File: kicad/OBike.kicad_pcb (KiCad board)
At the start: 2 copper layers, 60 x 60 mm, 59 parts, among them J1 Conn_01x04, J3 Conn_01x02, J4 Conn_01x03, J5 Conn_01x08, J7 Conn_01x04, J8 Micro_SD_Card_Det1, SW1 5_position_tactile, U1 DPS368XTSA1, U2 DS3231M, U3 MCP23017_SO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

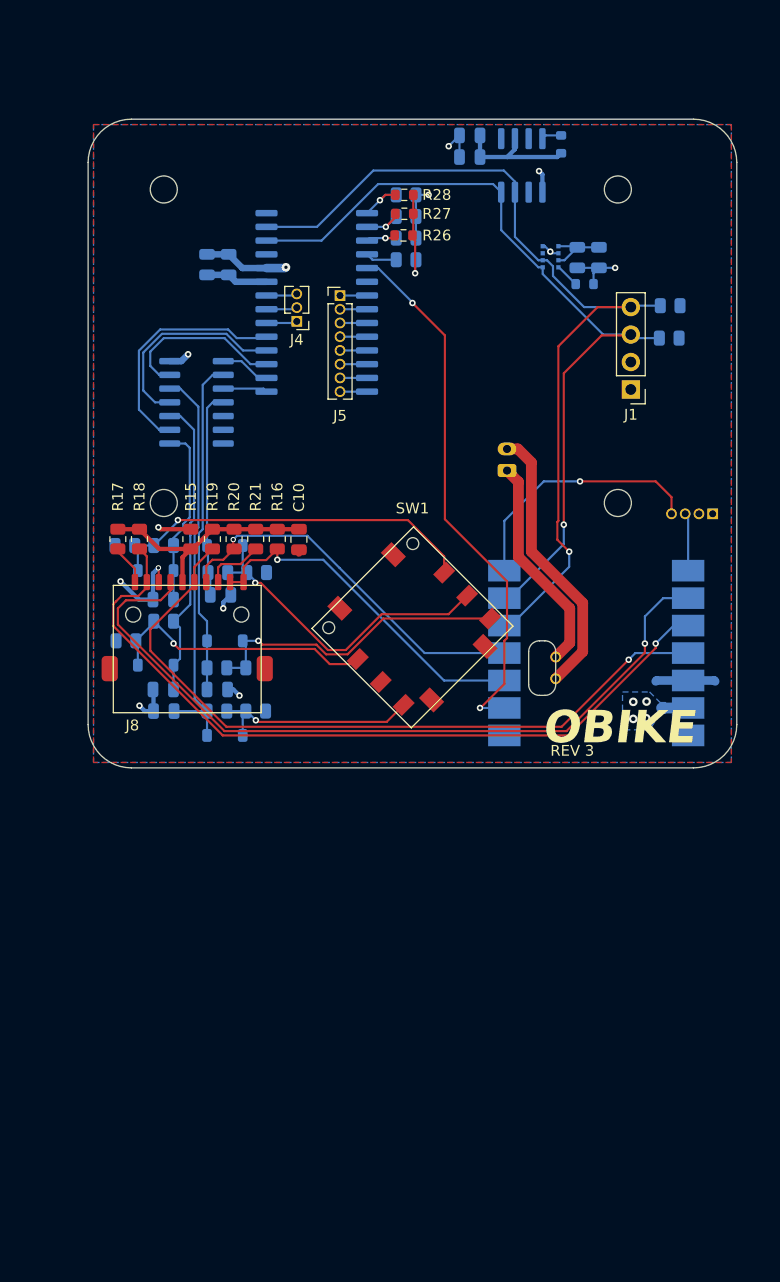
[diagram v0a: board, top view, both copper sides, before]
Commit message: 1.69" TFT
Changed screen connections to suit an SPI screen
Changed the arduino project to use the adafruit ST7789 library
Intended LCD is the wavshare 1.69" LCD
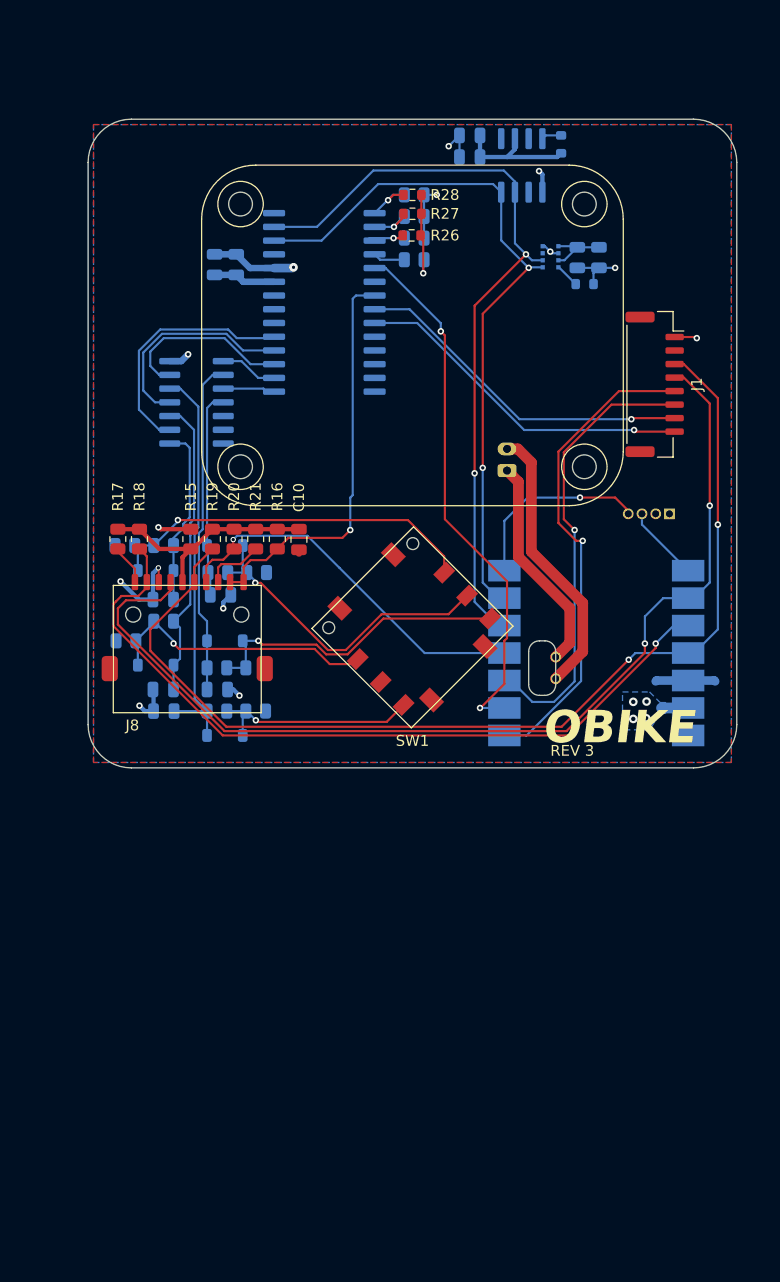
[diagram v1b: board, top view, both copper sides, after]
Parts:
- removed J4: Conn_01x03, Connector_PinHeader_1.27mm:PinHeader_1x03_P1.27mm_Vertical
- removed J5: Conn_01x08, Connector_PinHeader_1.27mm:PinHeader_1x08_P1.27mm_Vertical
- removed R11, R12: 10K, Resistor_SMD:R_0805_2012Metric
- J1: value Conn_01x04 -> Conn_01x08; footprint Connector_PinHeader_2.54mm:PinHeader_1x04_P2.54mm_Vertical -> Connector_JST:JST_GH_SM08B-GHS-TB_1x08-1MP_P1.25mm_Horizontal
- moved J7 4.00 mm to (176.3, 82.0)
- moved J1 2.25 mm to (174.9, 70.0), turned to -90 degrees
- moved R22 0.75 mm to (152.7, 58.5)
- moved R23 0.75 mm to (152.7, 52.5)
- moved R24 0.75 mm to (152.7, 54.5)
- moved R25 0.75 mm to (152.7, 56.5)
- moved R26 0.75 mm to (152.4, 56.2)
- moved R27 0.75 mm to (152.5, 54.2)
- moved R28 0.75 mm to (152.5, 52.5)
- moved C11 0.70 mm to (136.2, 59.0)
- moved C12 0.70 mm to (134.2, 59.0)
- moved U3 0.70 mm to (144.3, 62.4)
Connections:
- net CS renamed SD_CS
- J1 pad 3: SCL -> MOSI
- J1 pad 4: SDA -> SCK
- U3 pad 21: Net-(J5-Pin_1) -> DET
- U3 pad 22: Net-(J5-Pin_2) -> SCR_RST
- U3 pad 23: Net-(J5-Pin_3) -> SCR_BL
- U3 pad 24: Net-(J5-Pin_4) -> unconnected-(U3-GPA3-Pad24)
- U3 pad 25: Net-(J5-Pin_5) -> unconnected-(U3-GPA4-Pad25)
- U3 pad 26: Net-(J5-Pin_6) -> unconnected-(U3-GPA5-Pad26)
- U3 pad 27: Net-(J5-Pin_7) -> unconnected-(U3-GPA6-Pad27)
- U3 pad 28: Net-(J5-Pin_8) -> unconnected-(U3-GPA7-Pad28)
- U5 pad 1: unconnected-(U5-PA02_A0_D0-Pad1) -> SCR_CS
- U5 pad 3: DET -> SCR_DC
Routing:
- net SCR_CS: track 0.00 -> 44.8 mm, vias 0 -> 1
- net SCR_DC: track 0.00 -> 41.8 mm, vias 0 -> 1
- net SCR_RST: track 0.00 -> 32.7 mm, vias 0 -> 1
- net SCR_BL: track 0.00 -> 32.6 mm, vias 0 -> 1
- net MOSI: track 67.3 -> 97.6 mm, vias 1 -> 2
- net SCK: track 71.7 -> 95.1 mm, vias 1 -> 2
- net SDA: track 86.1 -> 72.3 mm, vias 1 -> 2
- net SCL: track 77.9 -> 67.0 mm, vias 1 -> 2
- net TX: track 23.7 -> 17.8 mm
- net DET: track 33.3 -> 37.0 mm
- net Net-(J4-Pin_3): track 2.86 -> 0.00 mm
- net Net-(J4-Pin_2): track 2.86 -> 0.00 mm
- net Net-(J4-Pin_1): track 2.86 -> 0.00 mm
- net Net-(J5-Pin_8): track 2.50 -> 0.00 mm
- net Net-(J5-Pin_7): track 2.50 -> 0.00 mm
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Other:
- outline, holes or cut-outs redrawn

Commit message: gps added
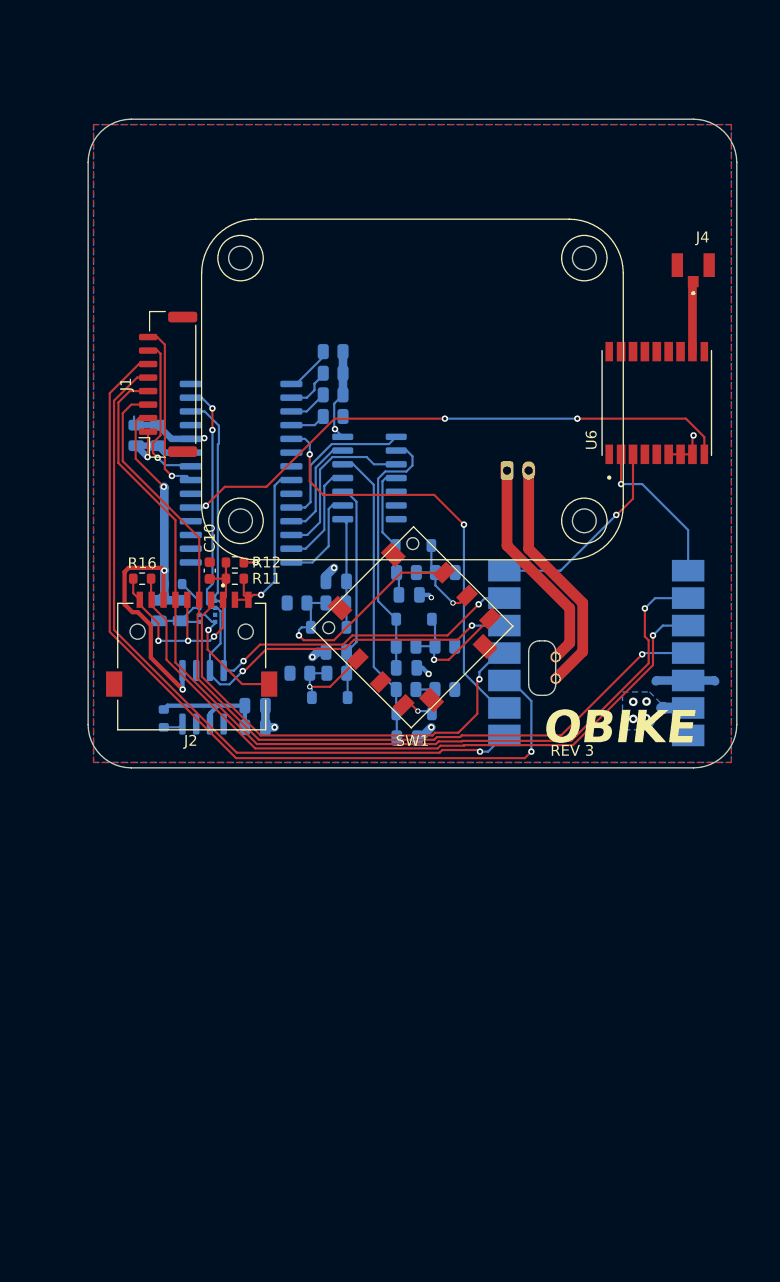
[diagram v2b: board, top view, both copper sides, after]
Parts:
- removed J7: Conn_01x04, Connector_PinHeader_1.27mm:PinHeader_1x04_P1.27mm_Vertical
- removed J8: Micro_SD_Card_Det1, CUI-devices:MSD-11-A
- removed R15: 2R2, Resistor_SMD:R_0805_2012Metric
- removed R17, R18, R19, R20, R21: 10K, Resistor_SMD:R_0805_2012Metric
- removed R26, R27, R28: 0R, Resistor_SMD:R_0603_1608Metric
- added J2: Micro_SD_Card_Det1, CUI-devices:CUI_MSD-11-A, F.Cu at (132.1, 96.1)
- added J4: 2337019-1, TE Connectivity:TE_2337019-1, F.Cu at (178.5, 59.0)
- added R11: 100K, Resistor_SMD:R_0603_1608Metric, F.Cu at (136.1, 88.0)
- added R12: 2R2, Resistor_SMD:R_0603_1608Metric, F.Cu at (136.1, 86.5)
- added U6: MAX-M8C-0, uBlox:XCVR_MAX-M8C-0, F.Cu at (175.1, 71.8)
- C10: footprint Capacitor_SMD:C_0805_2012Metric -> Capacitor_SMD:C_0603_1608Metric
- R16: value 100K -> 10K; footprint Resistor_SMD:R_0805_2012Metric -> Resistor_SMD:R_0603_1608Metric
- moved R13 64.6 mm to (129.5, 100.9), turned to 90 degrees
- moved C2 58.2 mm to (137.9, 101.8), turned to 0 degrees
- moved U2 57.4 mm to (133.1, 99.0), turned to 90 degrees
- moved C1 54.5 mm to (137.9, 99.8), turned to 0 degrees
- moved C4 52.2 mm to (129.1, 91.0), turned to 90 degrees
- moved C3 49.1 mm to (131.1, 91.0), turned to 90 degrees
- moved R14 47.1 mm to (130.4, 88.5), turned to 180 degrees
- moved U1 45.6 mm to (133.5, 91.0), turned to 90 degrees
- moved J1 45.0 mm to (129.9, 70.0), turned to 90 degrees
- moved C5 22.6 mm to (152.0, 102.8), turned to 0 degrees
- moved C8 17.6 mm to (151.9, 96.2)
- moved D1 17.6 mm to (152.7, 100.5)
- moved D4 17.6 mm to (152.7, 91.8)
- moved R1 17.6 mm to (155.5, 98.2)
- moved R2 17.6 mm to (151.9, 98.2)
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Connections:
- net Net-(J4-Pin_1) renamed GPS_RST
- R16 pad 2: DET -> MISO
- U3 pad 1: IN5 -> unconnected-(U3-GPB0-Pad1)
- U3 pad 2: IN4 -> unconnected-(U3-GPB1-Pad2)
- U3 pad 21: DET -> unconnected-(U3-GPA0-Pad21)
- U3 pad 22: SCR_RST -> DET
- U3 pad 23: SCR_BL -> unconnected-(U3-GPA2-Pad23)
- U3 pad 24: unconnected-(U3-GPA3-Pad24) -> IN4
- U3 pad 25: unconnected-(U3-GPA4-Pad25) -> IN1
- U3 pad 26: unconnected-(U3-GPA5-Pad26) -> IN5
- U3 pad 27: unconnected-(U3-GPA6-Pad27) -> IN2
- U3 pad 28: unconnected-(U3-GPA7-Pad28) -> IN3
- U3 pad 3: IN1 -> unconnected-(U3-GPB2-Pad3)
- U3 pad 4: IN2 -> unconnected-(U3-GPB3-Pad4)
- U3 pad 5: IN3 -> GPS_FO
- U3 pad 7: Net-(J4-Pin_2) -> SCR_BL
- U3 pad 8: Net-(J4-Pin_3) -> SCR_RST
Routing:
- net GPS_FO: track 0.00 -> 53.2 mm, vias 0 -> 3
- net GND: track 44.9 -> 83.9 mm
- net SCR_DC: track 41.8 -> 78.8 mm
- net SCR_CS: track 44.8 -> 66.8 mm
- net SW6: track 30.0 -> 9.50 mm
- net DET: track 37.0 -> 17.1 mm
- net SCR_RST: track 32.7 -> 14.8 mm
- net SW4: track 28.9 -> 12.2 mm
- net SCR_BL: track 32.6 -> 16.2 mm
- net MOSI: track 97.6 -> 81.2 mm, vias 2 -> 1
- net SW2: track 25.7 -> 9.43 mm
- net SDA: track 72.3 -> 57.9 mm, vias 2 -> 4
- net IN3: track 22.1 -> 8.50 mm
- net SW1: track 20.2 -> 7.09 mm
- net SW3: track 35.0 -> 22.1 mm
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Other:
- outline, holes or cut-outs redrawn

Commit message: antennae
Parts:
- J4, U6: moved to B.Cu
- moved J1 5.03 mm to (129.9, 65.0)
- moved J4 4.51 mm to (179.0, 54.5), turned to 90 degrees
- moved U6 3.94 mm to (173.9, 68.0)
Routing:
- net 3V3: track 38.1 -> 200.7 mm, vias 3 -> 2
- net GPS_FO: track 53.2 -> 131.2 mm, vias 3 -> 2
- net ANT: track 6.35 -> 15.5 mm
- net GND: track 83.9 -> 92.2 mm, vias 16 -> 17
- net SCR_CS: track 66.8 -> 72.3 mm
- net SCR_BL: track 16.2 -> 21.2 mm
- net SCK: track 89.0 -> 93.9 mm
- net SCR_DC: track 78.8 -> 83.5 mm
- net MOSI: track 81.2 -> 86.0 mm
- net SCR_RST: track 14.8 -> 19.4 mm
- net TX: track 18.8 -> 21.9 mm, vias 1 -> 2
- net RX: track 14.5 -> 14.8 mm, vias 1 -> 0
- removed copper zone on B.Cu, net 3V3
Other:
- outline, holes or cut-outs redrawn

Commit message: gps 4-layer
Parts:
- removed J4: 2337019-1, TE Connectivity:TE_2337019-1
- added AE1: Antenna, Antenna:AC30036-01, F.Cu at (182.8, 38.6)
- moved U6 8.17 mm to (174.4, 59.9)
- moved J1 5.00 mm to (129.9, 60.0)
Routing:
- net 3V3: track 200.7 -> 46.1 mm, vias 2 -> 18
- net GPS_FO: track 131.2 -> 59.6 mm, vias 2 -> 0
- net GND: track 92.2 -> 67.6 mm, vias 17 -> 23
- net TX: track 21.9 -> 35.5 mm, vias 2 -> 0
- net RX: track 14.8 -> 22.8 mm
- net MOSI: track 86.0 -> 91.7 mm
- net SCR_BL: track 21.2 -> 26.3 mm
- net SCR_RST: track 19.4 -> 24.4 mm
- net SCK: track 93.9 -> 98.3 mm
- net SCR_DC: track 83.5 -> 87.7 mm
- net SCR_CS: track 72.3 -> 76.0 mm
- net ANT: track 15.5 -> 18.4 mm
- net SDA: track 57.9 -> 60.3 mm, vias 4 -> 2
- net Net-(J2-DAT1): track 24.7 -> 23.1 mm
- net SD_CS: track 42.9 -> 43.5 mm
- added copper zone on In1.Cu, net 3V3
- added copper zone on In2.Cu, net GND
- removed copper zone on B.Cu, net GND
- removed copper zone on F.Cu, net GND
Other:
- board size 60 x 60 mm -> 60 x 69 mm
- copper layers 2 -> 4

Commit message: stopper using logger
also some fixes for tcx
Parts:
- moved C6 45.3 mm to (145.5, 140.0)
- moved R13 45.3 mm to (129.5, 146.2)
- moved AE1 45.3 mm to (182.8, 83.9)
- moved ? 45.2 mm to (165.8, 140.5)
- moved ? 45.2 mm to (165.8, 142.5)
- moved C1 45.2 mm to (137.9, 145.0)
- moved C10 45.2 mm to (133.8, 132.5)
- moved C11 45.2 mm to (128.9, 120.0)
- moved C12 45.2 mm to (127.0, 120.0)
- moved C2 45.2 mm to (137.9, 147.0)
- moved C5 45.2 mm to (152.0, 148.0)
- moved C7 45.2 mm to (145.4, 133.5)
- moved C8 45.2 mm to (151.9, 141.5)
- moved C9 45.2 mm to (152.2, 134.8)
- moved D1 45.2 mm to (152.7, 145.8)
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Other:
- board size 60 x 69 mm -> 60 x 109 mm

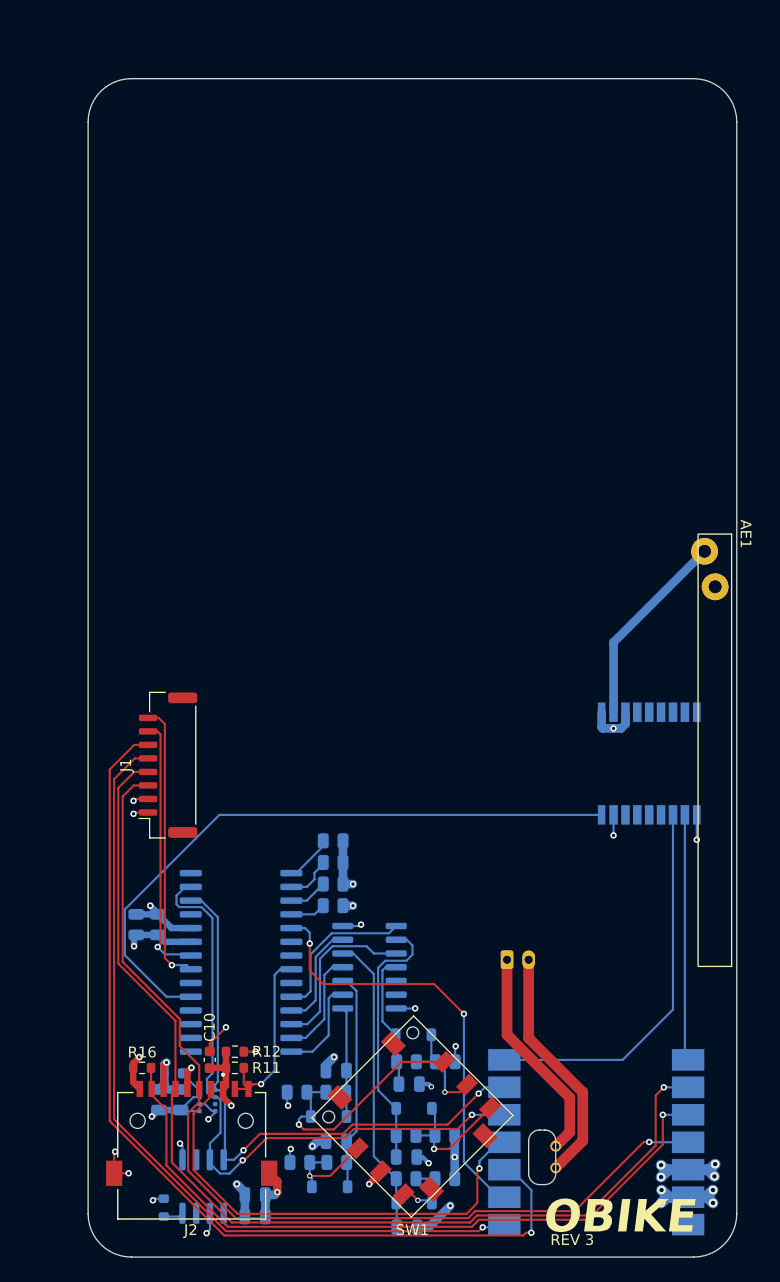
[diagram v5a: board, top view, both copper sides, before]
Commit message: quectel module
changed gps module
increased board size
moved gps module to front bottom left
moved sd card front bottom right
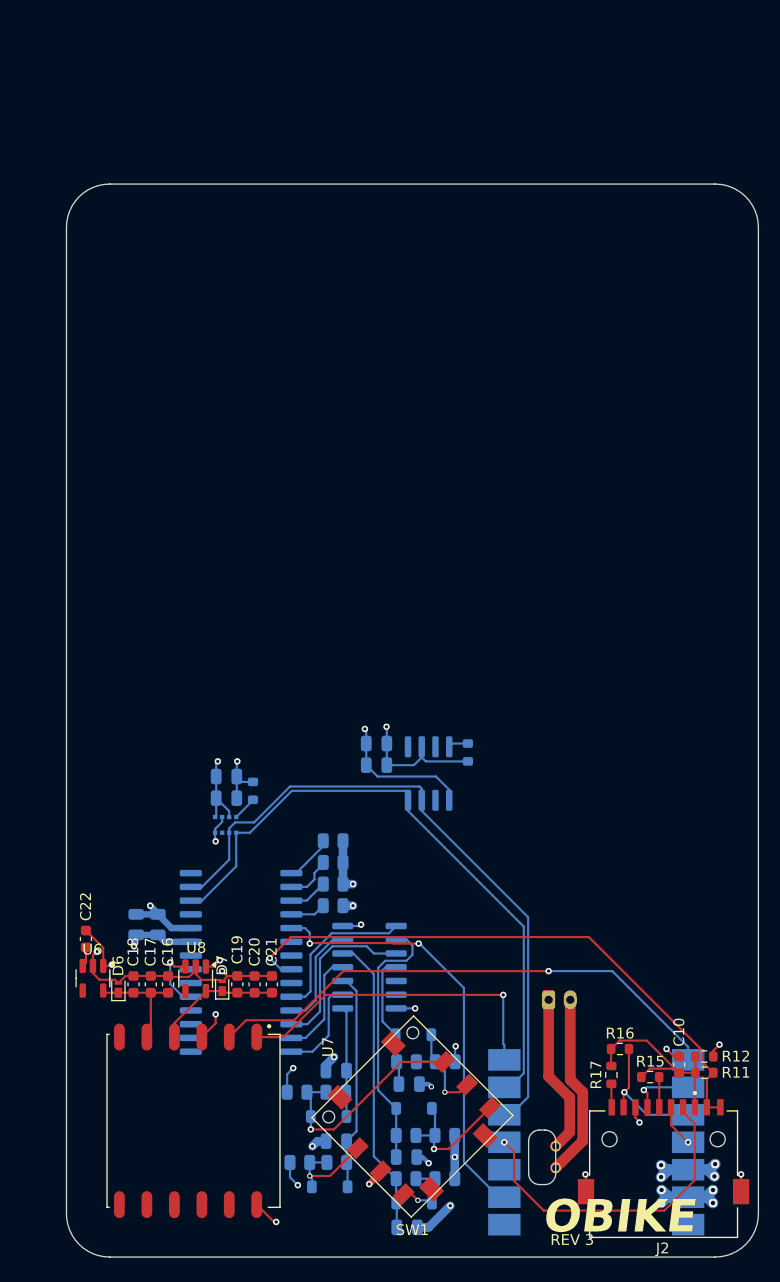
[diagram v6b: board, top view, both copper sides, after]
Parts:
- removed AE1: Antenna, Antenna:AC30036-01
- removed J1: Conn_01x08, Connector_JST:JST_GH_SM08B-GHS-TB_1x08-1MP_P1.25mm_Horizontal
- added C16: 33pF, Capacitor_SMD:C_0603_1608Metric, F.Cu at (129.9, 125.5)
- added C17: 100nF, Capacitor_SMD:C_0603_1608Metric, F.Cu at (128.3, 125.5)
- added C18: 4.7uF, Capacitor_SMD:C_0603_1608Metric, F.Cu at (126.7, 125.5)
- added C19: 10uF, Capacitor_SMD:C_0603_1608Metric, F.Cu at (136.3, 125.5)
- added C20: 100nF, Capacitor_SMD:C_0603_1608Metric, F.Cu at (137.9, 125.5)
- added C21: 33pF, Capacitor_SMD:C_0603_1608Metric, F.Cu at (139.5, 125.5)
- added C22: 10uF, Capacitor_SMD:C_0603_1608Metric, F.Cu at (122.3, 121.3)
- added D6: PTVS5V0Z1USK, Diode_SMD:Nexperia_DSN1608-2_1.6x0.8mm, F.Cu at (125.3, 126.0)
- added D7: PTVS5V0Z1USK, Diode_SMD:Nexperia_DSN1608-2_1.6x0.8mm, F.Cu at (134.9, 125.9)
- added R15: 100K, Resistor_SMD:R_0603_1608Metric, F.Cu at (174.5, 134.1)
- added R17: 100K, Resistor_SMD:R_0603_1608Metric, F.Cu at (170.9, 133.9)
- added U7: L86-M33, quectel:L86-M33, F.Cu at (131.8, 138.2)
- added U8: MAX40200AUK, Package_TO_SOT_SMD:SOT-23-5, F.Cu at (132.4, 125.0)
- R16: value 10K -> 100K
- U6: value MAX-M8C-0 -> MAX40200AUK; footprint uBlox:XCVR_MAX-M8C-0 -> Package_TO_SOT_SMD:SOT-23-5; moved to F.Cu
- moved U6 55.2 mm to (123.0, 125.0), turned to -90 degrees
- moved R13 50.6 mm to (157.6, 104.1), turned to -90 degrees
- moved C2 45.2 mm to (149.2, 103.2), turned to 180 degrees
- moved R16 44.2 mm to (171.7, 131.5)
- moved J2 43.7 mm to (175.7, 143.1)
- moved U2 43.5 mm to (154.0, 106.0), turned to -90 degrees
- moved C10 43.4 mm to (177.2, 132.9)
- moved R11 43.4 mm to (179.5, 133.7)
- moved R12 43.4 mm to (179.5, 132.2)
- moved C1 41.3 mm to (149.2, 105.2), turned to 180 degrees
- moved C4 30.5 mm to (135.3, 106.3), turned to 0 degrees
- moved C3 28.2 mm to (135.3, 108.3), turned to 0 degrees
- moved R14 27.1 mm to (137.8, 107.6), turned to 90 degrees
- moved U1 25.6 mm to (135.2, 110.8), turned to 0 degrees
- moved J3 5.34 mm to (165.1, 127.0)
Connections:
- C10 pad 1: Net-(J2-DAT1) -> Net-(J2-DAT2)
- J2 pad 1: Net-(J2-DAT1) -> Net-(J2-DAT2)
- J2 pad 4: Net-(J2-DAT1) -> Net-(J2-VDD)
- R11 pad 1: Net-(J2-DAT1) -> Net-(J2-DAT2)
- R12 pad 2: Net-(J2-DAT1) -> Net-(J2-DAT2)
- R16 pad 1: Net-(J2-DAT1) -> Net-(J2-DAT2)
- U3 pad 5: GPS_FO -> GPS_EN
- U6 pad 1: GND -> 3V3
- U6 pad 2: RX -> GND
- U6 pad 3: TX -> Net-(U6-EN)
- U6 pad 5: unconnected-(U6-EXTINT-Pad5) -> GPS_V_BKP
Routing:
- net SCK: track 98.3 -> 5.98 mm
- net MOSI: track 91.7 -> 3.88 mm
- net SCR_DC: track 87.7 -> 0.00 mm, vias 1 -> 0
- net SCR_CS: track 76.0 -> 0.00 mm, vias 1 -> 0
- net GPS_FO: track 59.6 -> 0.00 mm
- net MISO: track 66.1 -> 12.4 mm
- net DET: track 17.1 -> 54.8 mm
- net RX: track 22.8 -> 49.4 mm, vias 0 -> 1
- net SCR_BL: track 26.3 -> 0.00 mm, vias 1 -> 0
- net SCR_RST: track 24.4 -> 0.00 mm, vias 1 -> 0
- net GND: track 67.6 -> 90.4 mm, vias 23 -> 24
- net Net-(J2-DAT1): track 23.1 -> 2.19 mm, vias 3 -> 0
- net Net-(J2-DAT2): track 0.00 -> 19.7 mm
- net ANT: track 18.4 -> 0.00 mm
- net SD_CS: track 43.5 -> 30.1 mm
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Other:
- board size 60 x 109 mm -> 64 x 99.2 mm
